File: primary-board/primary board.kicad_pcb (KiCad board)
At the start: 4 copper layers, 92 x 82 mm, 45 parts, among them J1 USB_C, J10 Motor Connector Right, J2 Sensor_Forward, J3 Sensor_Right, J4 Sensor_Left, J5 I2C Breakout, J6 Conn_01x02, J7 Conn_01x02, J8 Conn_01x02, J9 Motor Connector Left, SW1 SW_SPST, SW2 SW_SPST, SW3 SW_SPDT, U1 ESP32-S3-1, U2 L7806, U3 L7806, U4 AZ1117-3.3, U5 DRV8411ARTER

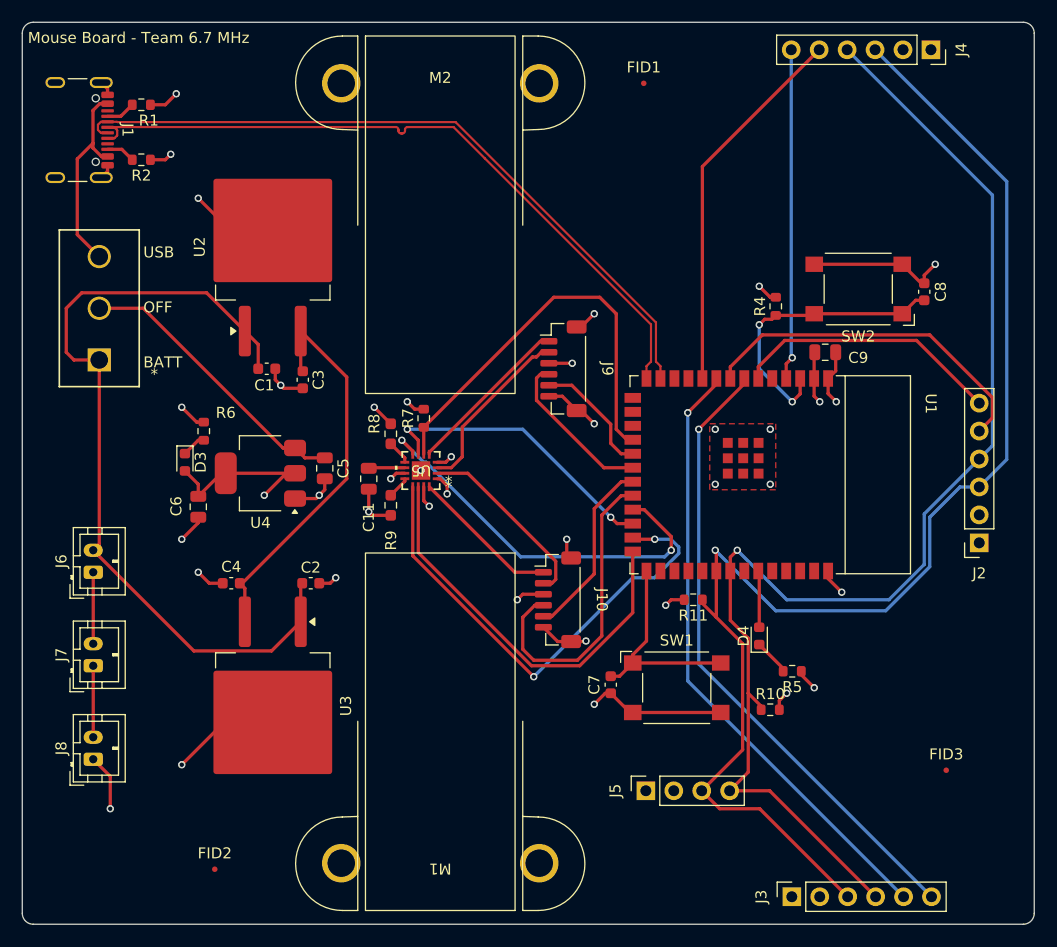
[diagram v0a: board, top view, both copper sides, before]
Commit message: removed digital sensors
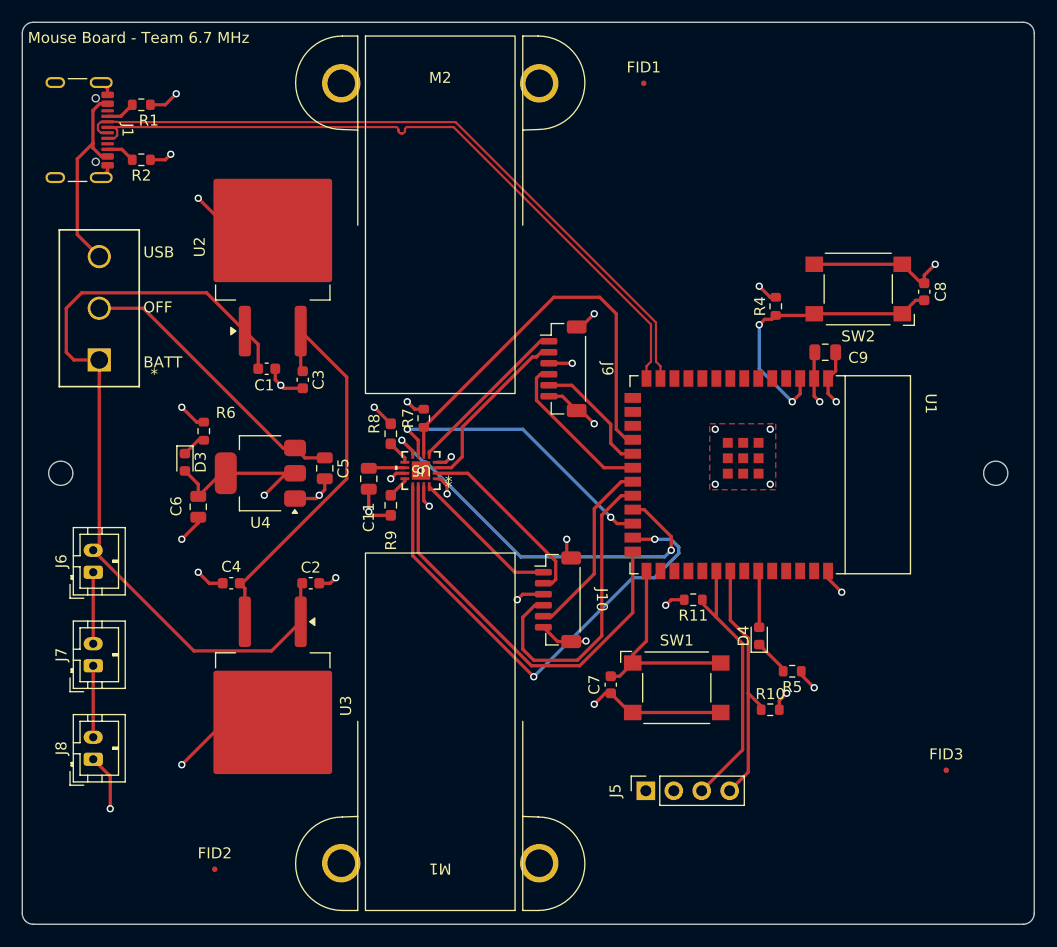
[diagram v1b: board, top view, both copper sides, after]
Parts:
- removed J2: Sensor_Forward, Connector_PinSocket_2.54mm:PinSocket_1x06_P2.54mm_Vertical
- removed J3: Sensor_Right, Connector_PinSocket_2.54mm:PinSocket_1x06_P2.54mm_Vertical
- removed J4: Sensor_Left, Connector_PinSocket_2.54mm:PinSocket_1x06_P2.54mm_Vertical
- added H1: MountingHole, MountingHole:MountingHole_2.2mm_M2, F.Cu at (192.0, 89.0)
- added H2: MountingHole, MountingHole:MountingHole_2.2mm_M2, F.Cu at (107.0, 89.0)
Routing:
- net /MCU_SCL: track 123.1 -> 24.6 mm, vias 1 -> 0
- net /MCU_SDA: track 117.8 -> 23.3 mm, vias 1 -> 0
- net /RIGHT_SHUTDOWN: track 57.6 -> 0.00 mm, vias 1 -> 0
- net /RIGHT_INT: track 56.3 -> 0.00 mm, vias 1 -> 0
- net /LEFT_INT: track 34.3 -> 0.00 mm
- net /FORWARD_INT: track 32.0 -> 0.00 mm
- net /LEFT_SHUTDOWN: track 30.2 -> 0.00 mm, vias 1 -> 0
- net /FORWARD_SHUTDOWN: track 24.5 -> 0.00 mm

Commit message: routed analog sensors
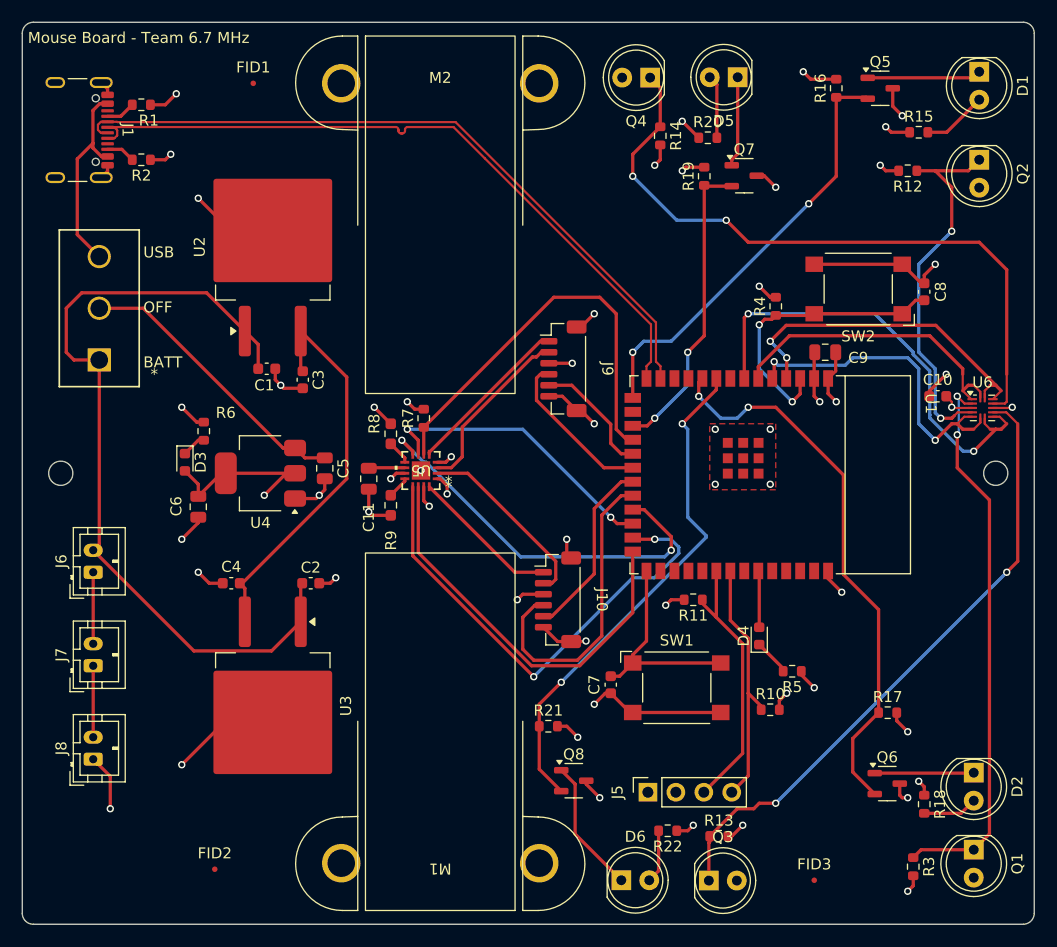
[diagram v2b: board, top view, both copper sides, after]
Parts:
- added C10: 0.1u, Capacitor_SMD:C_0603_1608Metric, F.Cu at (186.7, 82.0)
- added D1: INL-5AMIR15, LED_THT:LED_D5.0mm_IRGrey, F.Cu at (190.5, 52.5)
- added D2: INL-5AMIR15, LED_THT:LED_D5.0mm_IRGrey, F.Cu at (190.0, 116.2)
- added D5: INL-5AMIR15, LED_THT:LED_D5.0mm_IRGrey, F.Cu at (168.5, 53.0)
- added D6: INL-5AMIR15, LED_THT:LED_D5.0mm_IRGrey, F.Cu at (158.0, 126.0)
- added Q1: SFH 313 FA-3/4, LED_THT:LED_D5.0mm_IRGrey, F.Cu at (190.0, 123.2)
- added Q2: SFH 313 FA-3/4, LED_THT:LED_D5.0mm_IRGrey, F.Cu at (190.5, 60.5)
- added Q3: SFH 313 FA-3/4, LED_THT:LED_D5.0mm_IRGrey, F.Cu at (165.9, 126.0)
- added Q4: SFH 313 FA-3/4, LED_THT:LED_D5.0mm_IRGrey, F.Cu at (160.6, 53.0)
- added Q5: NMOS, Package_TO_SOT_SMD:SOT-23-3, F.Cu at (181.5, 54.0)
- added Q6: NMOS, Package_TO_SOT_SMD:SOT-23-3, F.Cu at (182.1, 117.2)
- added Q7: NMOS, Package_TO_SOT_SMD:SOT-23-3, F.Cu at (169.1, 62.0)
- added Q8: NMOS, Package_TO_SOT_SMD:SOT-23-3, F.Cu at (153.6, 117.0)
- added R12: 2.2k, Resistor_SMD:R_0603_1608Metric, F.Cu at (184.0, 61.5)
- added R13: 2.2k, Resistor_SMD:R_0603_1608Metric, F.Cu at (166.8, 122.0)
- added R14: 2.2k, Resistor_SMD:R_0603_1608Metric, F.Cu at (161.5, 58.3)
- added R15: 100, Resistor_SMD:R_0603_1608Metric, F.Cu at (185.0, 58.0)
- added R16: 4.7k, Resistor_SMD:R_0603_1608Metric, F.Cu at (177.5, 54.0)
- added R17: 4.7k, Resistor_SMD:R_0603_1608Metric, F.Cu at (182.2, 110.8)
- added R18: 100, Resistor_SMD:R_0603_1608Metric, F.Cu at (185.5, 119.1)
- added R19: 4.7k, Resistor_SMD:R_0603_1608Metric, F.Cu at (165.5, 62.0)
- added R20: 100, Resistor_SMD:R_0603_1608Metric, F.Cu at (165.8, 58.5)
- added R21: 4.7k, Resistor_SMD:R_0603_1608Metric, F.Cu at (151.3, 112.0)
- added R22: 100, Resistor_SMD:R_0603_1608Metric, F.Cu at (162.2, 121.5)
- added R3: 2.2k, Resistor_SMD:R_0603_1608Metric, F.Cu at (184.5, 124.8)
- added U6: TLV9004xRUCR, Package_DFN_QFN:Texas_S-PX2QFN-14, F.Cu at (190.8, 83.1)
- moved FID1 35.5 mm to (124.5, 53.5)
- moved FID3 15.6 mm to (175.5, 126.0)
- moved J5 0.23 mm to (160.4, 118.0)
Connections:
- net /MCU_SCL renamed MCU_SCL
- net /MCU_SDA renamed MCU_SDA
- U1 pad 10: /LEFT_INT -> ir_led_front_right
- U1 pad 15: unconnected-(U1-IO3-Pad15) -> ir_led_front_left
- U1 pad 17: unconnected-(U1-IO9-Pad17) -> ir_led_left
- U1 pad 4: /LEFT_SHUTDOWN -> analog_sense_left
- U1 pad 5: unconnected-(U1-IO5-Pad5) -> analog_sense_front_left
- U1 pad 6: /FORWARD_SHUTDOWN -> analog_sense_front_right
- U1 pad 7: /RIGHT_SHUTDOWN -> analog_sense_right
- U1 pad 8: /FORWARD_INT -> unconnected-(U1-IO15-Pad8)
- U1 pad 9: /RIGHT_INT -> ir_led_right
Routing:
- net Net-(U6D-+): track 0.00 -> 61.2 mm, vias 0 -> 2
- net Net-(U6C-+): track 0.00 -> 57.6 mm, vias 0 -> 2
- net ir_led_front_right: track 0.00 -> 50.8 mm, vias 0 -> 2
- net Net-(U6A-+): track 0.00 -> 50.6 mm, vias 0 -> 2
- net ir_led_right: track 0.00 -> 46.8 mm, vias 0 -> 2
- net analog_sense_right: track 0.00 -> 41.6 mm, vias 0 -> 2
- net ir_led_front_left: track 0.00 -> 39.4 mm, vias 0 -> 2
- net Net-(U6B-+): track 0.00 -> 34.4 mm, vias 0 -> 2
- net analog_sense_left: track 0.00 -> 31.0 mm, vias 0 -> 2
- net GND: track 107.7 -> 138.2 mm, vias 30 -> 44
- net analog_sense_front_left: track 0.00 -> 29.9 mm, vias 0 -> 2
- net ir_led_left: track 0.00 -> 27.9 mm, vias 0 -> 2
- net analog_sense_front_right: track 0.00 -> 27.8 mm
- net Net-(D6-K): track 0.00 -> 12.3 mm
- net +3.3V: track 34.9 -> 45.7 mm, vias 9 -> 14
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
